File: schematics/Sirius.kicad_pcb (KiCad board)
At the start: 2 copper layers, 6 parts, among them U1 W65C02SxP, U2 W65C51NxPL, U3 6526, U6 27C64, U7 CY62256-70PC, X1 GTXO-14T

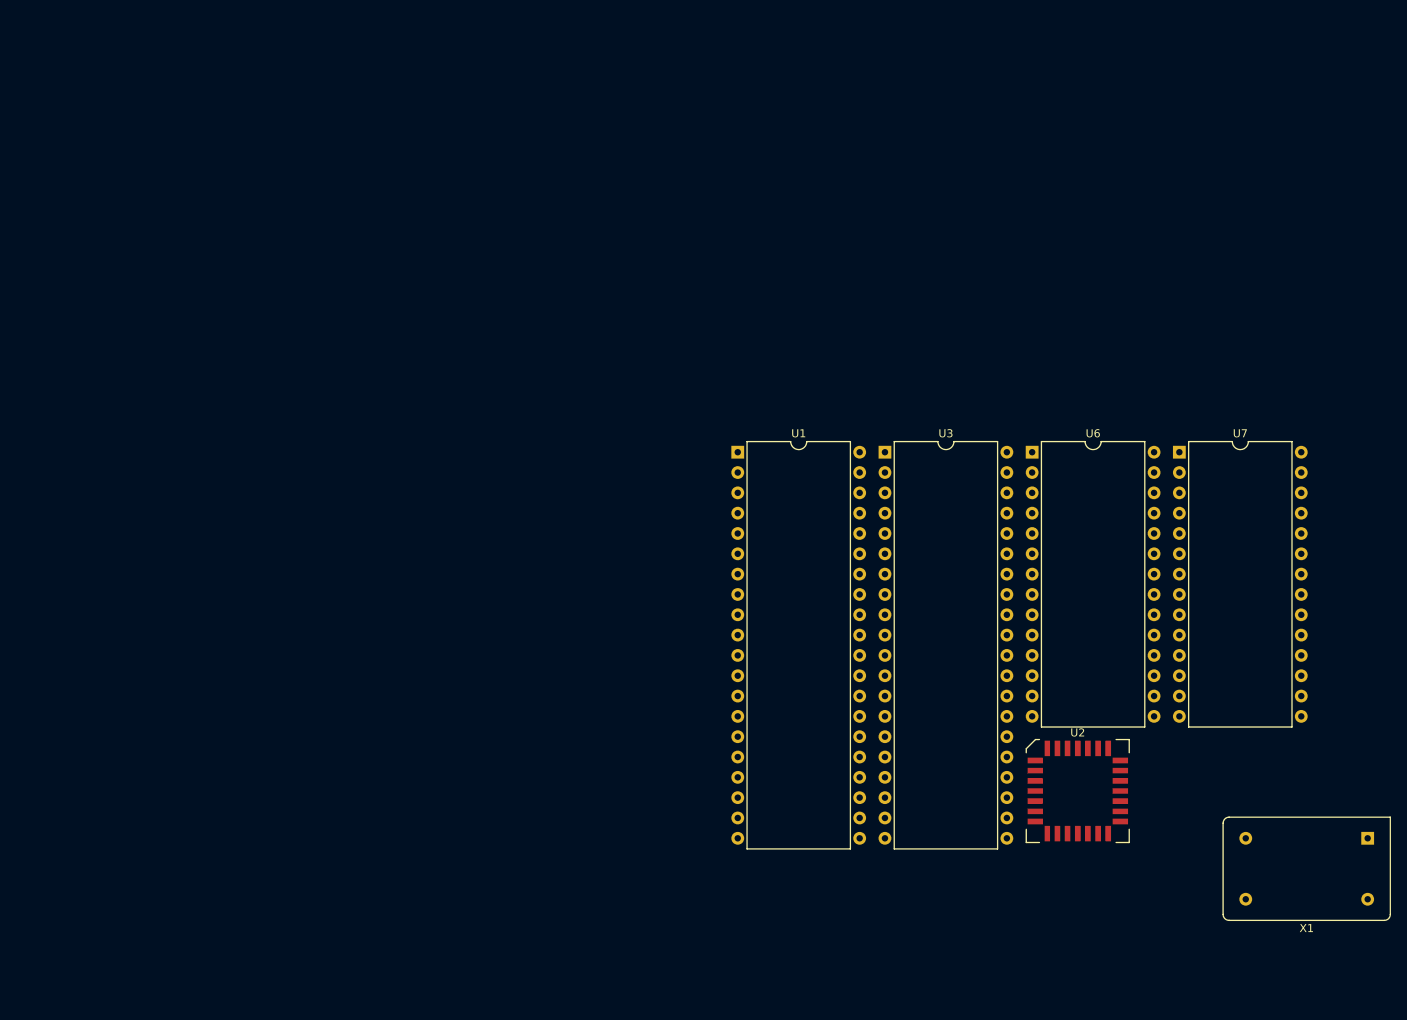
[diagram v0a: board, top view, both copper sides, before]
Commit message: Added RAM along with connectivity. Still issues with using the Bus.
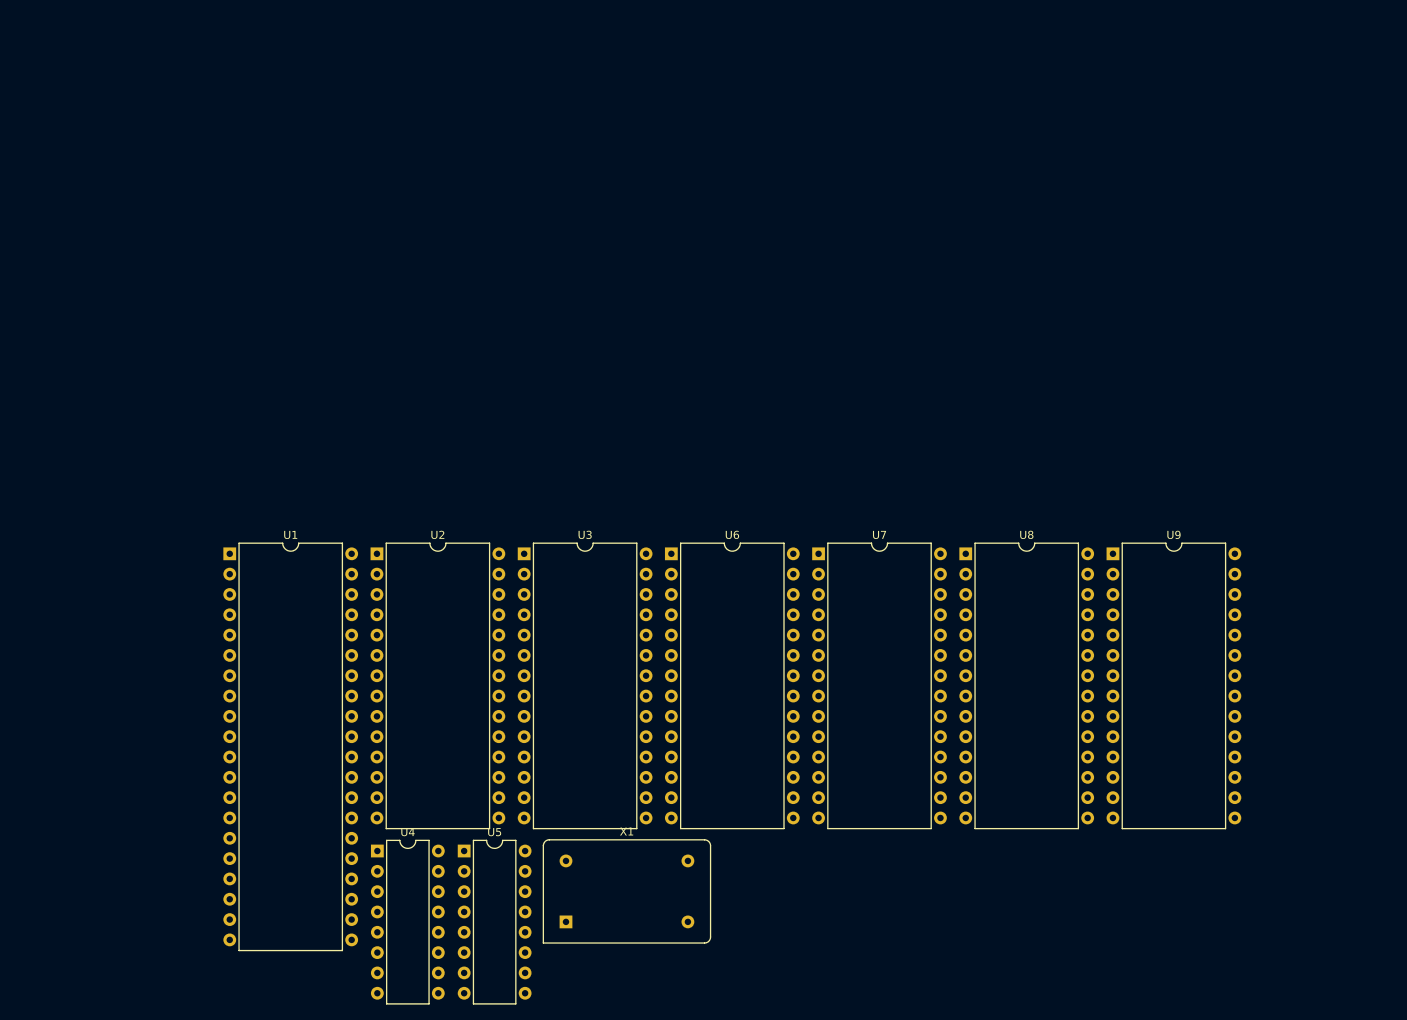
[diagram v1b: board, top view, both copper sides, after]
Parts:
- added U4: 74LS138, Package_DIP:DIP-16_W7.62mm, F.Cu at (56.5, 115.9)
- added U5: 74LS138, Package_DIP:DIP-16_W7.62mm, F.Cu at (67.4, 115.9)
- added U8: ~, Package_DIP:DIP-28_W15.24mm, F.Cu at (130.1, 78.7)
- added U9: ~, Package_DIP:DIP-28_W15.24mm, F.Cu at (148.5, 78.7)
- U2: value W65C51NxPL -> W65C51NxP; footprint Package_LCC:PLCC-28 -> Package_DIP:DIP-28_W15.24mm
- U3: value 6526 -> 2764; footprint Package_DIP:DIP-40_W15.24mm -> Package_DIP:DIP-28_W15.24mm
- U6: value 27C64 -> ~
- U7: value CY62256-70PC -> ~
- X1: value GTXO-14T -> TFT680
- moved X1 100.8 mm to (80.1, 124.8), turned to 0 degrees
- moved U2 92.5 mm to (56.5, 78.7)
- moved U1 64.8 mm to (38.1, 78.7)
- moved U6 46.9 mm to (93.3, 78.7)
- moved U7 46.9 mm to (111.7, 78.7)
- moved U3 46.9 mm to (74.9, 78.7)
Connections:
- U1 pad 10: /A1 -> unconnected-(U1-A1-Pad10)
- U1 pad 11: /A2 -> unconnected-(U1-A2-Pad11)
- U1 pad 12: /A3 -> unconnected-(U1-A3-Pad12)
- U1 pad 13: /A4 -> unconnected-(U1-A4-Pad13)
- U1 pad 14: /A5 -> unconnected-(U1-A5-Pad14)
- U1 pad 15: /A6 -> unconnected-(U1-A6-Pad15)
- U1 pad 16: /A7 -> unconnected-(U1-A7-Pad16)
- U1 pad 17: /A8 -> unconnected-(U1-A8-Pad17)
- U1 pad 18: /A9 -> unconnected-(U1-A9-Pad18)
- U1 pad 19: /A10 -> unconnected-(U1-A10-Pad19)
- U1 pad 20: /A11 -> unconnected-(U1-A11-Pad20)
- U1 pad 21: GND -> VSS
- U1 pad 22: /A12 -> unconnected-(U1-A12-Pad22)
- U1 pad 23: /A13 -> unconnected-(U1-A13-Pad23)
- U1 pad 24: /A14 -> unconnected-(U1-A14-Pad24)
- U1 pad 25: /A15 -> unconnected-(U1-A15-Pad25)
- U1 pad 26: /D7 -> unconnected-(U1-D7-Pad26)
- U1 pad 27: /D6 -> unconnected-(U1-D6-Pad27)
- U1 pad 28: /D5 -> unconnected-(U1-D5-Pad28)
- U1 pad 29: /D4 -> unconnected-(U1-D4-Pad29)
- U1 pad 30: /D3 -> unconnected-(U1-D3-Pad30)
- U1 pad 31: /D2 -> unconnected-(U1-D2-Pad31)
- U1 pad 32: /D1 -> unconnected-(U1-D1-Pad32)
- U1 pad 33: /D0 -> unconnected-(U1-D0-Pad33)
- U1 pad 37: unconnected-(U1-ϕ0-Pad37) -> Net-(U1-ϕ0)
- U1 pad 8: Vcc -> VDD
- U1 pad 9: /A0 -> unconnected-(U1-A0-Pad9)
- U2 pad 1: GND -> VSS
- U2 pad 15: Vcc -> VCC
- U2 pad 2: unconnected-(U2-CS1-Pad2) -> Net-(U2-CS1)
- U2 pad 3: unconnected-(U2-~{CS2}-Pad3) -> VSS
- U3 pad 1: GND -> unconnected-(U3-VPP-Pad1)
- U3 pad 14: unconnected-(U3-PB4-Pad14) -> GND
- U3 pad 20: Vcc -> Net-(U3-~{CE})
- U3 pad 21: Net-(U1-~{IRQ}) -> unconnected-(U3-A10-Pad21)
- U3 pad 25: Net-(U1-ϕ2) -> unconnected-(U3-A8-Pad25)
- U3 pad 28: unconnected-(U3-D5-Pad28) -> VCC
- U6 pad 10: /A0 -> unconnected-(U6-A12-Pad10)
- U6 pad 11: /D0 -> unconnected-(U6-I/O1-Pad11)
- U6 pad 12: /D1 -> unconnected-(U6-I/O1-Pad12)
- U6 pad 13: /D2 -> unconnected-(U6-I/O2-Pad13)
- U6 pad 15: /D3 -> unconnected-(U6-I/O3-Pad15)
- U6 pad 16: /D4 -> unconnected-(U6-I/O4-Pad16)
- U6 pad 17: /D5 -> unconnected-(U6-I/O5-Pad17)
- U6 pad 18: /D6 -> unconnected-(U6-I/O6-Pad18)
- U6 pad 19: /D7 -> unconnected-(U6-I/O7-Pad19)
- U6 pad 2: /A12 -> unconnected-(U6-A4-Pad2)
- U6 pad 21: /A10 -> unconnected-(U6-A0-Pad21)
- U6 pad 23: /A11 -> unconnected-(U6-A1-Pad23)
- U6 pad 24: /A9 -> unconnected-(U6-A2-Pad24)
- U6 pad 25: /A8 -> unconnected-(U6-A3-Pad25)
- U6 pad 27: unconnected-(U6-~{PGM}-Pad27) -> Net-(U1-R/~{W})
- U6 pad 28: Vcc -> VCC
- U6 pad 3: /A7 -> unconnected-(U6-A5-Pad3)
- U6 pad 4: /A6 -> unconnected-(U6-A6-Pad4)
- U6 pad 5: /A5 -> unconnected-(U6-A7-Pad5)
- U6 pad 6: /A4 -> unconnected-(U6-A8-Pad6)
- U6 pad 7: /A3 -> unconnected-(U6-A9-Pad7)
- U6 pad 8: /A2 -> unconnected-(U6-A10-Pad8)
- U6 pad 9: /A1 -> unconnected-(U6-A11-Pad9)
- U7 pad 1: /A14 -> unconnected-(U7-NC-Pad1)
- U7 pad 10: /A0 -> unconnected-(U7-A12-Pad10)
- U7 pad 2: /A12 -> unconnected-(U7-A4-Pad2)
- U7 pad 21: /A10 -> unconnected-(U7-A0-Pad21)
- U7 pad 23: /A11 -> unconnected-(U7-A1-Pad23)
- U7 pad 24: /A9 -> unconnected-(U7-A2-Pad24)
- U7 pad 25: /A8 -> unconnected-(U7-A3-Pad25)
- U7 pad 26: /A13 -> unconnected-(U7-CE2-Pad26)
- U7 pad 28: Vcc -> VCC
- U7 pad 3: /A7 -> unconnected-(U7-A5-Pad3)
- U7 pad 4: /A6 -> unconnected-(U7-A6-Pad4)
- U7 pad 5: /A5 -> unconnected-(U7-A7-Pad5)
- U7 pad 6: /A4 -> unconnected-(U7-A8-Pad6)
- U7 pad 7: /A3 -> unconnected-(U7-A9-Pad7)
- U7 pad 8: /A2 -> unconnected-(U7-A10-Pad8)
- U7 pad 9: /A1 -> unconnected-(U7-A11-Pad9)
- X1 pad 1: unconnected-(X1-EN-Pad1) -> VCC
- X1 pad 14: Vcc -> VCC
- X1 pad 8: Net-(U1-ϕ2) -> Net-(U1-ϕ0)

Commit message: Added rs232 parts. Still some caps to add.
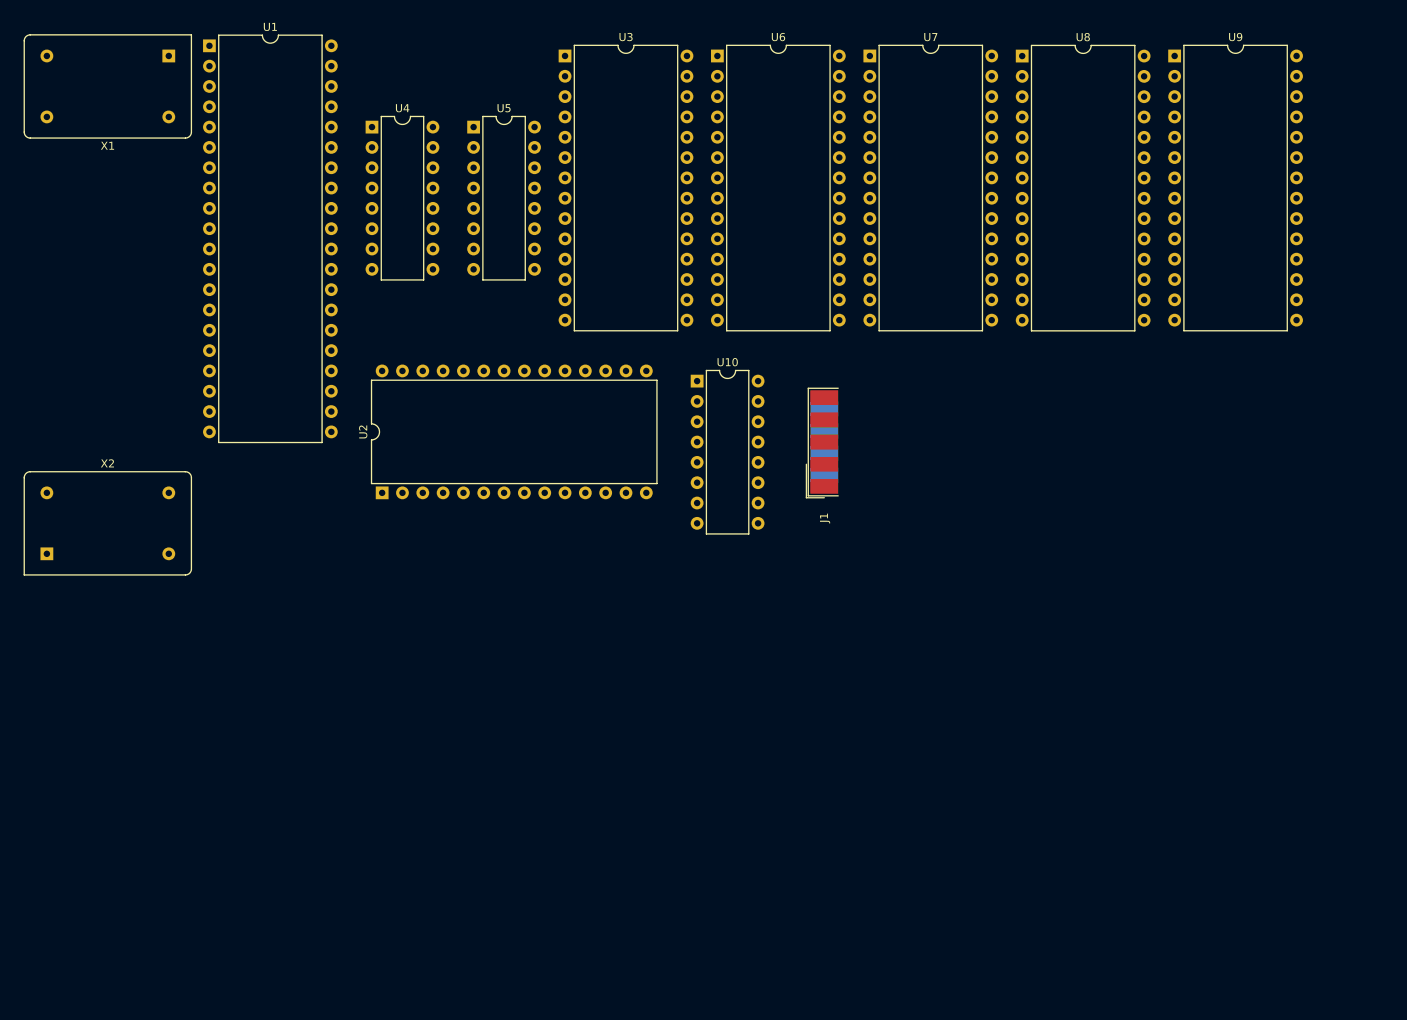
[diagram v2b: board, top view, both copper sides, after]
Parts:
- added J1: DE9_Plug, Connector_Dsub:DSUB-9_Male_EdgeMount_P2.77mm, F.Cu at (112.4, 64.8)
- added U10: MAX232, Package_DIP:DIP-16_W7.62mm, F.Cu at (96.5, 57.1)
- added X2: TFT680, Oscillator:Oscillator_DIP-14, F.Cu at (15.2, 78.7)
- moved X1 119.1 mm to (30.5, 16.5), turned to 180 degrees
- moved U5 90.5 mm to (68.6, 25.4)
- moved U4 90.5 mm to (55.9, 25.4)
- moved U1 63.6 mm to (35.6, 15.2)
- moved U9 62.7 mm to (156.2, 16.5)
- moved U8 62.6 mm to (137.2, 16.5)
- moved U7 62.6 mm to (118.1, 16.5)
- moved U6 62.5 mm to (99.1, 16.5)
- moved U3 62.4 mm to (80.0, 16.5)
- moved U2 7.65 mm to (57.1, 71.1), turned to 90 degrees
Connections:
- U2 pad 10: unconnected-(U2-TxD-Pad10) -> Net-(U10-T1IN)
- U2 pad 11: unconnected-(U2-~{DTR}-Pad11) -> Net-(U2-~{DTR})
- U2 pad 12: unconnected-(U2-RxD-Pad12) -> Net-(U10-R1OUT)
- U2 pad 17: unconnected-(U2-~{DSR}-Pad17) -> Net-(U2-~{DSR})
- U2 pad 8: unconnected-(U2-~{RTS}-Pad8) -> Net-(U2-~{RTS})
- U2 pad 9: unconnected-(U2-~{CTS}-Pad9) -> Net-(U2-~{CTS})
- U4 pad 12: unconnected-(U4-O3-Pad12) -> Net-(U4-O3)
- U4 pad 13: unconnected-(U4-O2-Pad13) -> Net-(U4-O2)
- U4 pad 14: unconnected-(U4-O1-Pad14) -> Net-(U4-O1)
- U4 pad 15: unconnected-(U4-O0-Pad15) -> Net-(U4-O0)
- U6 pad 20: unconnected-(U6-/CE1-Pad20) -> Net-(U4-O0)
- U6 pad 26: unconnected-(U6-CE2-Pad26) -> VCC
- U7 pad 20: unconnected-(U7-/CE1-Pad20) -> Net-(U4-O1)
- U7 pad 26: unconnected-(U7-CE2-Pad26) -> VCC
- U8 pad 20: unconnected-(U8-/CE1-Pad20) -> Net-(U4-O2)
- U8 pad 26: unconnected-(U8-CE2-Pad26) -> VCC
- U9 pad 20: unconnected-(U9-/CE1-Pad20) -> Net-(U4-O3)
- U9 pad 26: unconnected-(U9-CE2-Pad26) -> VCC

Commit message: Minor tweaks to signals and PCB layout.
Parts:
- moved X2 59.2 mm to (38.1, 24.1)
- moved J1 46.9 mm to (132.1, 22.2), turned to 180 degrees
- moved U10 43.8 mm to (118.1, 19.1), turned to -90 degrees
- moved U2 40.8 mm to (61.0, 30.5)
- moved U5 35.1 mm to (45.7, 52.1)
- moved U6 29.8 mm to (76.2, 35.6)
- moved U3 29.8 mm to (57.1, 35.6)
- moved U9 29.8 mm to (133.3, 35.6)
- moved U7 29.8 mm to (95.2, 35.6)
- moved U8 29.7 mm to (114.3, 35.6)
- moved U1 26.4 mm to (14.0, 30.5)
- moved U4 22.9 mm to (34.3, 33.0)

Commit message: Fixed the Bus connetions. Added a forgotten 7404 inverter for R/W signal and did a autorouted board.
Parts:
- added U11: 7404, Package_DIP:DIP-14_W7.62mm, F.Cu at (34.3, 59.7)
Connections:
- U1 pad 10: unconnected-(U1-A1-Pad10) -> A1
- U1 pad 11: unconnected-(U1-A2-Pad11) -> A2
- U1 pad 12: unconnected-(U1-A3-Pad12) -> A3
- U1 pad 13: unconnected-(U1-A4-Pad13) -> A4
- U1 pad 14: unconnected-(U1-A5-Pad14) -> A5
- U1 pad 15: unconnected-(U1-A6-Pad15) -> A6
- U1 pad 16: unconnected-(U1-A7-Pad16) -> A7
- U1 pad 17: unconnected-(U1-A8-Pad17) -> A8
- U1 pad 18: unconnected-(U1-A9-Pad18) -> A9
- U1 pad 19: unconnected-(U1-A10-Pad19) -> A10
- U1 pad 2: unconnected-(U1-RDY-Pad2) -> VDD
- U1 pad 20: unconnected-(U1-A11-Pad20) -> A11
- U1 pad 22: unconnected-(U1-A12-Pad22) -> A12
- U1 pad 23: unconnected-(U1-A13-Pad23) -> A13
- U1 pad 24: unconnected-(U1-A14-Pad24) -> A14
- U1 pad 25: unconnected-(U1-A15-Pad25) -> A15
- U1 pad 26: unconnected-(U1-D7-Pad26) -> /D7
- U1 pad 27: unconnected-(U1-D6-Pad27) -> /D6
- U1 pad 28: unconnected-(U1-D5-Pad28) -> /D5
- U1 pad 29: unconnected-(U1-D4-Pad29) -> /D4
- U1 pad 30: unconnected-(U1-D3-Pad30) -> /D3
- U1 pad 31: unconnected-(U1-D2-Pad31) -> /D2
- U1 pad 32: unconnected-(U1-D1-Pad32) -> /D1
- U1 pad 33: unconnected-(U1-D0-Pad33) -> /D0
- U1 pad 36: unconnected-(U1-BE-Pad36) -> VDD
- U1 pad 9: unconnected-(U1-A0-Pad9) -> A0
- U10 pad 1: unconnected-(U10-C1+-Pad1) -> Net-(U10-C1+)
- U10 pad 3: unconnected-(U10-C1--Pad3) -> Net-(U10-C1-)
- U10 pad 4: unconnected-(U10-C2+-Pad4) -> Net-(U10-C2+)
- U10 pad 5: unconnected-(U10-C2--Pad5) -> Net-(U10-C2-)
- U2 pad 13: unconnected-(U2-RS0-Pad13) -> A0
- U2 pad 14: unconnected-(U2-RS1-Pad14) -> A1
- U2 pad 18: unconnected-(U2-D0-Pad18) -> /D0
- U2 pad 19: unconnected-(U2-D1-Pad19) -> /D1
- U2 pad 20: unconnected-(U2-D2-Pad20) -> /D2
- U2 pad 21: unconnected-(U2-D3-Pad21) -> /D3
- U2 pad 22: unconnected-(U2-D4-Pad22) -> /D4
- U2 pad 23: unconnected-(U2-D5-Pad23) -> /D5
- U2 pad 24: unconnected-(U2-D6-Pad24) -> /D6
- U2 pad 25: unconnected-(U2-D7-Pad25) -> /D7
- U2 pad 6: unconnected-(U2-XTAL1-Pad6) -> Net-(U2-XTAL1)
- U3 pad 10: unconnected-(U3-A0-Pad10) -> A0
- U3 pad 11: unconnected-(U3-D0-Pad11) -> /D0
- U3 pad 12: unconnected-(U3-D1-Pad12) -> /D1
- U3 pad 13: unconnected-(U3-D2-Pad13) -> /D2
- U3 pad 15: unconnected-(U3-D3-Pad15) -> /D3
- U3 pad 16: unconnected-(U3-D4-Pad16) -> /D4
- U3 pad 17: unconnected-(U3-D5-Pad17) -> /D5
- U3 pad 18: unconnected-(U3-D6-Pad18) -> /D6
- U3 pad 19: unconnected-(U3-D7-Pad19) -> /D7
- U3 pad 2: unconnected-(U3-A12-Pad2) -> A12
- U3 pad 21: unconnected-(U3-A10-Pad21) -> A10
- U3 pad 23: unconnected-(U3-A11-Pad23) -> A11
- U3 pad 24: unconnected-(U3-A9-Pad24) -> A9
- U3 pad 25: unconnected-(U3-A8-Pad25) -> A8
- U3 pad 3: unconnected-(U3-A7-Pad3) -> A7
- U3 pad 4: unconnected-(U3-A6-Pad4) -> A5
- U3 pad 5: unconnected-(U3-A5-Pad5) -> A5
- U3 pad 6: unconnected-(U3-A4-Pad6) -> A4
- U3 pad 7: unconnected-(U3-A3-Pad7) -> A3
- U3 pad 8: unconnected-(U3-A2-Pad8) -> A2
- U3 pad 9: unconnected-(U3-A1-Pad9) -> A1
- U4 pad 1: unconnected-(U4-A0-Pad1) -> A0
- U4 pad 2: unconnected-(U4-A1-Pad2) -> A1
- U4 pad 3: unconnected-(U4-A2-Pad3) -> A2
- U5 pad 1: unconnected-(U5-A0-Pad1) -> A0
- U5 pad 2: unconnected-(U5-A1-Pad2) -> A1
- U5 pad 3: unconnected-(U5-A2-Pad3) -> A2
- U6 pad 10: unconnected-(U6-A12-Pad10) -> A12
- U6 pad 11: unconnected-(U6-I/O1-Pad11) -> /D0
- U6 pad 12: unconnected-(U6-I/O1-Pad12) -> /D1
- U6 pad 13: unconnected-(U6-I/O2-Pad13) -> /D2
- U6 pad 15: unconnected-(U6-I/O3-Pad15) -> /D3
- U6 pad 16: unconnected-(U6-I/O4-Pad16) -> /D4
- U6 pad 17: unconnected-(U6-I/O5-Pad17) -> /D5
- U6 pad 18: unconnected-(U6-I/O6-Pad18) -> /D6
- U6 pad 19: unconnected-(U6-I/O7-Pad19) -> /D7
- U6 pad 2: unconnected-(U6-A4-Pad2) -> A4
- U6 pad 21: unconnected-(U6-A0-Pad21) -> A0
- U6 pad 22: unconnected-(U6-/OE-Pad22) -> Net-(U6-/OE)
- U6 pad 23: unconnected-(U6-A1-Pad23) -> A1
- U6 pad 24: unconnected-(U6-A2-Pad24) -> A2
- U6 pad 25: unconnected-(U6-A3-Pad25) -> A3
- U6 pad 3: unconnected-(U6-A5-Pad3) -> A5
- U6 pad 4: unconnected-(U6-A6-Pad4) -> A6
- U6 pad 5: unconnected-(U6-A7-Pad5) -> A7
- U6 pad 6: unconnected-(U6-A8-Pad6) -> A8
- U6 pad 7: unconnected-(U6-A9-Pad7) -> A9
- U6 pad 8: unconnected-(U6-A10-Pad8) -> A10
- U6 pad 9: unconnected-(U6-A11-Pad9) -> A11
- U7 pad 10: unconnected-(U7-A12-Pad10) -> A12
- U7 pad 11: unconnected-(U7-I/O1-Pad11) -> /D0
- U7 pad 12: unconnected-(U7-I/O1-Pad12) -> /D1
- U7 pad 13: unconnected-(U7-I/O2-Pad13) -> /D2
- U7 pad 15: unconnected-(U7-I/O3-Pad15) -> /D3
- U7 pad 16: unconnected-(U7-I/O4-Pad16) -> /D4
- U7 pad 17: unconnected-(U7-I/O5-Pad17) -> /D5
- U7 pad 18: unconnected-(U7-I/O6-Pad18) -> /D6
- U7 pad 19: unconnected-(U7-I/O7-Pad19) -> /D7
- U7 pad 2: unconnected-(U7-A4-Pad2) -> A4
- U7 pad 21: unconnected-(U7-A0-Pad21) -> A0
- U7 pad 22: unconnected-(U7-/OE-Pad22) -> Net-(U6-/OE)
- U7 pad 23: unconnected-(U7-A1-Pad23) -> A1
- U7 pad 24: unconnected-(U7-A2-Pad24) -> A2
- U7 pad 25: unconnected-(U7-A3-Pad25) -> A3
- U7 pad 3: unconnected-(U7-A5-Pad3) -> A5
- U7 pad 4: unconnected-(U7-A6-Pad4) -> A6
- U7 pad 5: unconnected-(U7-A7-Pad5) -> A7
- U7 pad 6: unconnected-(U7-A8-Pad6) -> A8
- U7 pad 7: unconnected-(U7-A9-Pad7) -> A9
- U7 pad 8: unconnected-(U7-A10-Pad8) -> A10
- U7 pad 9: unconnected-(U7-A11-Pad9) -> A11
- U8 pad 10: unconnected-(U8-A12-Pad10) -> A12
- U8 pad 11: unconnected-(U8-I/O1-Pad11) -> /D0
- U8 pad 12: unconnected-(U8-I/O1-Pad12) -> /D1
- U8 pad 13: unconnected-(U8-I/O2-Pad13) -> /D2
- U8 pad 15: unconnected-(U8-I/O3-Pad15) -> /D3
- U8 pad 16: unconnected-(U8-I/O4-Pad16) -> /D4
- U8 pad 17: unconnected-(U8-I/O5-Pad17) -> /D5
- U8 pad 18: unconnected-(U8-I/O6-Pad18) -> /D6
- U8 pad 19: unconnected-(U8-I/O7-Pad19) -> /D7
- U8 pad 2: unconnected-(U8-A4-Pad2) -> A4
- U8 pad 21: unconnected-(U8-A0-Pad21) -> A0
- U8 pad 22: unconnected-(U8-/OE-Pad22) -> Net-(U6-/OE)
- U8 pad 23: unconnected-(U8-A1-Pad23) -> A1
- U8 pad 24: unconnected-(U8-A2-Pad24) -> A2
- U8 pad 25: unconnected-(U8-A3-Pad25) -> A3
- U8 pad 3: unconnected-(U8-A5-Pad3) -> A5
- U8 pad 4: unconnected-(U8-A6-Pad4) -> A6
- U8 pad 5: unconnected-(U8-A7-Pad5) -> A7
- U8 pad 6: unconnected-(U8-A8-Pad6) -> A8
- U8 pad 7: unconnected-(U8-A9-Pad7) -> A9
- U8 pad 8: unconnected-(U8-A10-Pad8) -> A10
- U8 pad 9: unconnected-(U8-A11-Pad9) -> A11
- U9 pad 10: unconnected-(U9-A12-Pad10) -> A12
- U9 pad 11: unconnected-(U9-I/O1-Pad11) -> /D0
- U9 pad 12: unconnected-(U9-I/O1-Pad12) -> /D1
- U9 pad 13: unconnected-(U9-I/O2-Pad13) -> /D2
- U9 pad 15: unconnected-(U9-I/O3-Pad15) -> /D3
- U9 pad 16: unconnected-(U9-I/O4-Pad16) -> /D4
- U9 pad 17: unconnected-(U9-I/O5-Pad17) -> /D5
- U9 pad 18: unconnected-(U9-I/O6-Pad18) -> /D6
- U9 pad 19: unconnected-(U9-I/O7-Pad19) -> /D7
- U9 pad 2: unconnected-(U9-A4-Pad2) -> A4
- U9 pad 21: unconnected-(U9-A0-Pad21) -> A0
- U9 pad 22: unconnected-(U9-/OE-Pad22) -> Net-(U6-/OE)
- U9 pad 23: unconnected-(U9-A1-Pad23) -> A1
- U9 pad 24: unconnected-(U9-A2-Pad24) -> A2
- U9 pad 25: unconnected-(U9-A3-Pad25) -> A3
- U9 pad 3: unconnected-(U9-A5-Pad3) -> A5
- U9 pad 4: unconnected-(U9-A6-Pad4) -> A6
- U9 pad 5: unconnected-(U9-A7-Pad5) -> A7
- U9 pad 6: unconnected-(U9-A8-Pad6) -> A8
- U9 pad 7: unconnected-(U9-A9-Pad7) -> A9
- U9 pad 8: unconnected-(U9-A10-Pad8) -> A10
- U9 pad 9: unconnected-(U9-A11-Pad9) -> A11
- X2 pad 8: unconnected-(X2-OUT-Pad8) -> Net-(U2-XTAL1)
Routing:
- net GND: track 0.00 -> 279.4 mm
- net VCC: track 0.00 -> 265.8 mm, vias 0 -> 1
- net A2: track 0.00 -> 216.5 mm
- net A12: track 0.00 -> 212.5 mm, vias 0 -> 2
- net /D3: track 0.00 -> 204.8 mm
- net /D1: track 0.00 -> 198.8 mm, vias 0 -> 3
- net /D6: track 0.00 -> 192.5 mm, vias 0 -> 4
- net /D4: track 0.00 -> 191.4 mm, vias 0 -> 1
- net /D7: track 0.00 -> 190.8 mm, vias 0 -> 3
- net A0: track 0.00 -> 187.4 mm
- net /D0: track 0.00 -> 186.2 mm, vias 0 -> 2
- net /D5: track 0.00 -> 182.8 mm
- net A1: track 0.00 -> 179.7 mm
- net Net-(U1-R/~{W}): track 0.00 -> 179.4 mm, vias 0 -> 4
- net Net-(U4-O3): track 0.00 -> 176.1 mm
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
